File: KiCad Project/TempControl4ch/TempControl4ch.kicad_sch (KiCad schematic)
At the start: 76 parts, among them J1 Conn_01x08_Socket, J2 Conn_01x02_Socket, U1 MAX31856, U2 MAX31856, U3 MAX31856, U4 MAX31856, U5 BluePill_Part_Like_SWD_Breako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, U6 TPS54202DDC

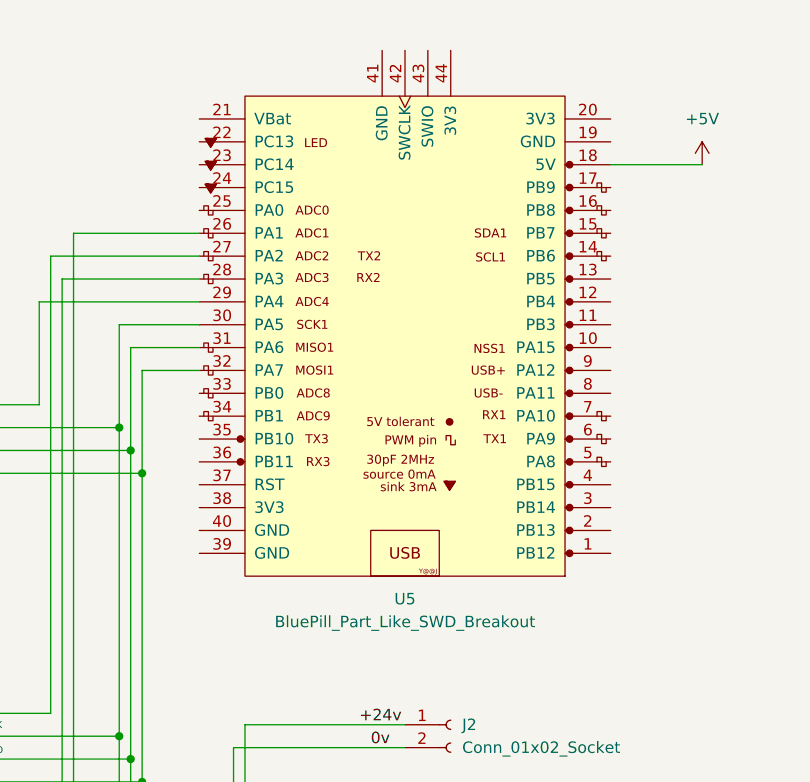
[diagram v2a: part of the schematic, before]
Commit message: update supply circuit pcb design
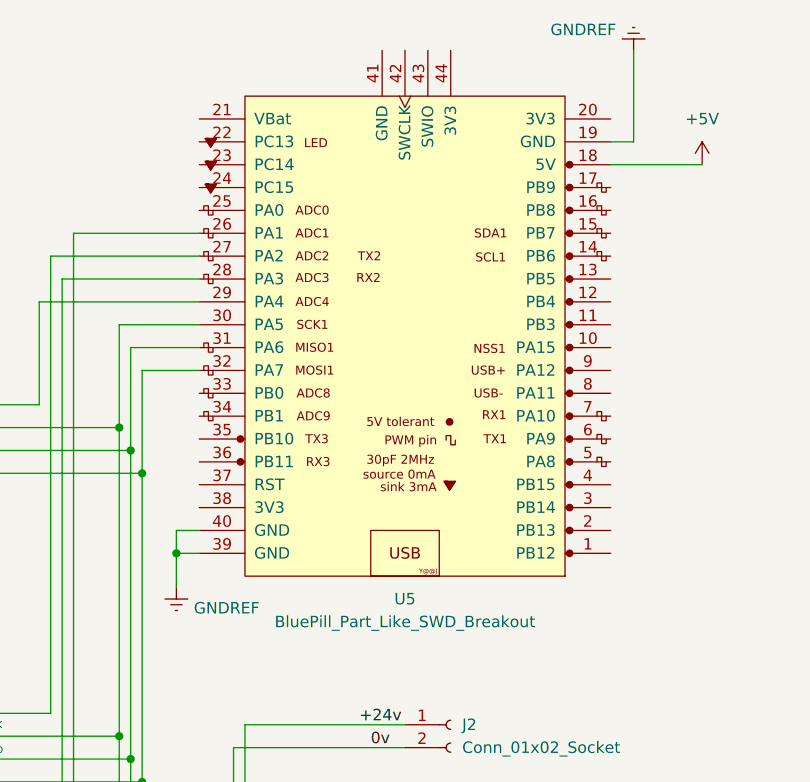
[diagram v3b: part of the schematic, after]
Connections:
- net GNDREF: now also U5.19 (GND), U5.39 (GND), U5.40 (GND)
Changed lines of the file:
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@@
 	)
 	(junction
+		(at 278.13 81.28)
+		(diameter 0)
+		(color 0 0 0 0)
+	)
+	(junction
 		(at 378.46 121.92)
 		(diameter 0)
@@
 	(wire
 		(pts
+			(xy 278.13 78.74) (xy 278.13 81.28)
+		)
+		(stroke
+			(width 0)
+			(type default)
+		)
+	)
+	(wire
+		(pts
 			(xy 199.39 165.1) (xy 207.01 165.1)
 		)
@@
 	(wire
 		(pts
+			(xy 328.93 25.4) (xy 328.93 35.56)
+		)
+		(stroke
+			(width 0)
+			(type default)
+		)
+	)
+	(wire
+		(pts
 			(xy 194.31 153.67) (xy 199.39 153.67)
 		)
@@
 	(wire
 		(pts
+			(xy 328.93 35.56) (xy 326.39 35.56)
+		)
+		(stroke
+			(width 0)
+			(type default)
+		)
+	)
+	(wire
+		(pts
 			(xy 161.29 158.75) (xy 157.48 158.75)
 		)
@@
 	(wire
 		(pts
+			(xy 280.67 78.74) (xy 278.13 78.74)
+		)
+		(stroke
+			(width 0)
+			(type default)
+		)
+	)
+	(wire
+		(pts
 			(xy 271.78 190.5) (xy 271.78 148.59)
 		)
@@
 	(wire
 		(pts
+			(xy 278.13 81.28) (xy 278.13 85.09)
+		)
+		(stroke
+			(width 0)
+			(type default)
+		)
+	)
+	(wire
+		(pts
 			(xy 111.76 205.74) (xy 116.84 205.74)
 		)
@@
 	(wire
 		(pts
+			(xy 278.13 81.28) (xy 280.67 81.28)
+		)
+		(stroke
+			(width 0)
+			(type default)
+		)
+	)
+	(wire
+		(pts
 			(xy 162.56 77.47) (xy 158.75 77.47)
 		)
@@
 	)
 	(symbol
+		(lib_id "power:GNDREF")
+		(at 278.13 85.09 0)
+		(unit 1)
+		(exclude_from_sim no)
+		(in_bom yes)
+		(on_board yes)
+		(dnp no)
+		(property "Reference" "#PWR036"
+			(at 278.13 91.44 0)
+			(effects
+				(font
+					(size 1.27 1.27)
+				)
+				(hide yes)
+			)
+		)
+		(property "Value" "GNDREF"
+			(at 283.718 87.376 0)
+			(effects
+				(font
+					(size 1.27 1.27)
+				)
+			)
+		)
+		(property "Footprint" ""
+			(at 278.13 85.09 0)
+			(effects
+				(font
+					(size 1.27 1.27)
+				)
+				(hide yes)
+			)
+		)
+		(property "Datasheet" ""
+			(at 278.13 85.09 0)
+			(effects
+				(font
+					(size 1.27 1.27)
+				)
+				(hide yes)
+			)
+		)
+		(property "Description" "Power symbol creates a global label with name \"GNDREF\" , reference supply ground"
+			(at 278.13 85.09 0)
+			(effects
+				(font
+					(size 1.27 1.27)
+				)
+				(hide yes)
+			)
+		)
+		(pin "1"
+		)
+		(instances
+			(project "TempControl4ch"
+				(path "/bfcf5f5c-9721-40d4-a7af-7e2f1fa1b9b1"
+					(reference "#PWR036")
+					(unit 1)
+				)
+			)
+		)
+	)
+	(symbol
 		(lib_id "Device:C")
 		(at 288.29 120.65 0)
@@
 					(unit 1)
 				)
+			)
+		)
+	)
+	(symbol
+		(lib_id "power:GNDREF")
+		(at 328.93 25.4 180)
+		(unit 1)
+		(exclude_from_sim no)
+		(in_bom yes)
+		(on_board yes)
+		(dnp no)
+		(property "Reference" "#PWR037"
+			(at 328.93 19.05 0)
+			(effects
+				(font
+					(size 1.27 1.27)
+				)
+				(hide yes)
+			)
+		)
+		(property "Value" "GNDREF"
+			(at 323.342 23.114 0)
+			(effects
+				(font
+					(size 1.27 1.27)
+				)
+			)
+		)
+		(property "Footprint" ""
+			(at 328.93 25.4 0)
+			(effects
+				(font
+					(size 1.27 1.27)
+				)
+				(hide yes)
+			)
+		)
+		(property "Datasheet" ""
+			(at 328.93 25.4 0)
+			(effects
+				(font
+					(size 1.27 1.27)
+				)
+				(hide yes)
+			)
+		)
+		(property "Description" "Power symbol creates a global label with name \"GNDREF\" , reference supply ground"
+			(at 328.93 25.4 0)
+			(effects
+				(font
+					(size 1.27 1.27)
+				)
+				(hide yes)
+			)
+		)
+		(pin "1"
+		)
+		(instances
+			(project "TempControl4ch"
+				(path "/bfcf5f5c-9721-40d4-a7af-7e2f1fa1b9b1"
+					(reference "#PWR037")
+					(unit 1)
+				)
